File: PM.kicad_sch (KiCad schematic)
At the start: 70 parts, among them Q1 SISA14DN-T1-GE3, Q13 MMBT3904, Q2 SISA14DN-T1-GE3, Q3 SISA14DN-T1-GE3, Q4 SISA14DN-T1-GE3, Q5 CEM4435A, Q6 CH221K, SW2 SKRKAEE020, U10 LM74700QDBVRQ1, U11 CN3795, U12 XFL4020-222MEC_C122469, U4 MAX17049G+T10, U5 LM74700QDBVRQ1, U6 LM74700QDBVRQ1, U7 TPS62132RGTT, U8 LM74700QDBVRQ1, U9 XC6209F332MR-G

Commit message: [Schematic][Added] Project Architecture, connectors
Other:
- moved on the sheet: C13, C14, C15, C16, C17, C18, C19, C2, C20, C3, C37, C4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

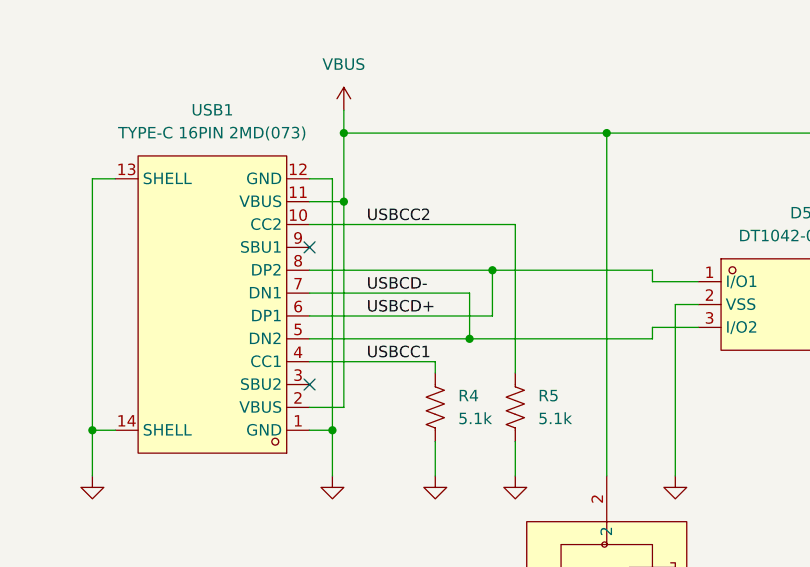
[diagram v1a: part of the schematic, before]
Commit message: [Schematic][Added] Net labels
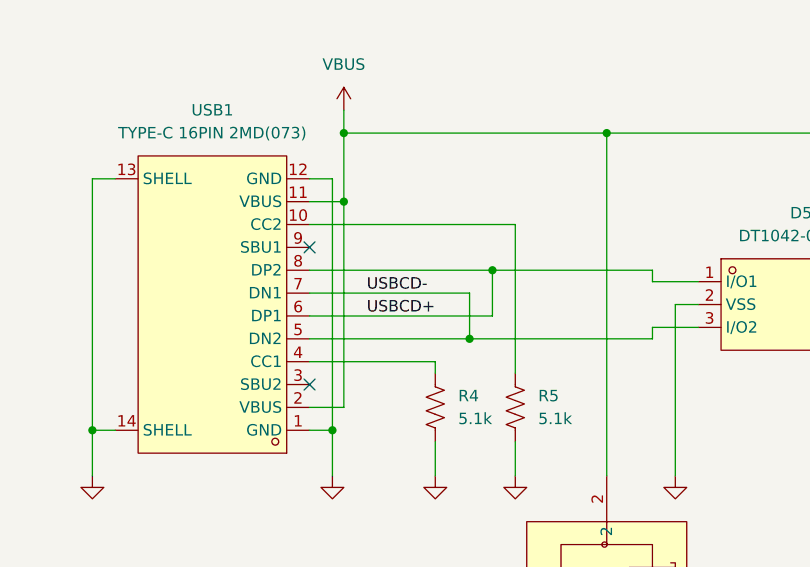
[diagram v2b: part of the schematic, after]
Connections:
- net USBCC1: no longer R4.1, USB1.4 (CC1)
- net USBCC2: no longer R5.1, USB1.10 (CC2)
- new net: R4.1, USB1.4 (CC1)
- new net: R5.1, USB1.10 (CC2)
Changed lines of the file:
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@@
-		)
-	)
-	(label "USBCC2"
-		(at 74.93 77.47 0)
-		(effects
-			(font
-				(size 1.27 1.27)
-			)
-			(justify left bottom)
 		)
 	)
@@
 		(effects
 			(font
-				(size 1.27 1.27)
-			)
-			(justify left bottom)
-		)
-	)
-	(label "USBCC1"
-		(at 74.93 92.71 0)
-		(effects
-			(font

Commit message: [PCB/SCH][Added] Preliminary version
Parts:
- removed C2, C3: 100u, Capacitor_SMD:C_1210_3225Metric, symbol Device:C
- C5: footprint Capacitor_SMD:C_0603_1608Metric -> Capacitor_SMD:C_0402_1005Metric
- R4, R5, R59, R60: footprint Resistor_SMD:R_0603_1608Metric -> Resistor_SMD:R_0402_1005Metric
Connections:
- net USBCC1: now also R4.1, USB1.4 (CC1)
- net USBCC2: now also R5.1, USB1.10 (CC2)
- net VBUS: no longer D5.5 (VCC)
- net V_BAT: now also C39.1, U9.1 (VIN), U9.3 (CE)
- net V_IN renamed V_CHRG

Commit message: [Schematic/PCB][Added] Connectors, layout, preliminar routing
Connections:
- net USBCD+: now also D5.3 (I/O2); no longer D5.1 (I/O1)
- net USBCD-: now also D5.1 (I/O1); no longer D5.3 (I/O2)
- net USBCC1 renamed CC1
- net USBCC2 renamed CC2
- no-connect marks 9 -> 10
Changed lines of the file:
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@@
 	)
 	(no_connect
+		(at 134.62 86.36)
+	)
+	(no_connect
 		(at 438.15 241.3)
 	)
@@
 	)
 	(bus_entry
+		(at 524.51 276.86)
+		(size -2.54 2.54)
+		(stroke
+			(width 0)
+			(type default)
+		)
+	)
+	(bus_entry
 		(at 524.51 241.3)
 		(size -2.54 2.54)
@@
 	)
 	(bus_entry
+		(at 524.51 274.32)
+		(size -2.54 2.54)
+		(stroke
+			(width 0)
+			(type default)
+		)
+	)
+	(bus_entry
 		(at 524.51 257.81)
 		(size -2.54 2.54)
@@
 	(wire
 		(pts
+			(xy 106.68 88.9) (xy 111.76 88.9)
+		)
+		(stroke
+			(width 0)
+			(type default)
+		)
+	)
+	(wire
+		(pts
 			(xy 502.92 73.66) (xy 514.35 73.66)
 		)
@@
 	(wire
 		(pts
-			(xy 106.68 83.82) (xy 106.68 82.55)
-		)
-		(stroke
-			(width 0)
-			(type default)
-		)
-	)
-	(wire
-		(pts
 			(xy 281.94 96.52) (xy 281.94 148.59)
 		)
@@
 	(wire
 		(pts
+			(xy 506.73 279.4) (xy 521.97 279.4)
+		)
+		(stroke
+			(width 0)
+			(type default)
+		)
+	)
+	(wire
+		(pts
 			(xy 269.24 154.94) (xy 271.78 154.94)
 		)
@@
 	(wire
 		(pts
+			(xy 107.95 83.82) (xy 111.76 83.82)
+		)
+		(stroke
+			(width 0)
+			(type default)
+		)
+	)
+	(wire
+		(pts
 			(xy 111.76 86.36) (xy 109.22 86.36)
 		)
@@
 	(wire
 		(pts
+			(xy 506.73 276.86) (xy 521.97 276.86)
+		)
+		(stroke
+			(width 0)
+			(type default)
+		)
+	)
+	(wire
+		(pts
 			(xy 236.22 90.17) (xy 240.03 90.17)
 		)
@@
 	(wire
 		(pts
-			(xy 438.15 233.68) (xy 440.69 233.68)
+			(xy 106.68 82.55) (xy 106.68 88.9)
 		)
 		(stroke
@@
 	(wire
 		(pts
-			(xy 252.73 247.65) (xy 252.73 245.11)
+			(xy 438.15 233.68) (xy 440.69 233.68)
 		)
 		(stroke
@@
 	(wire
 		(pts
-			(xy 271.78 106.68) (xy 269.24 106.68)
+			(xy 252.73 247.65) (xy 252.73 245.11)
 		)
 		(stroke
@@
 	(wire
 		(pts
-			(xy 270.51 295.91) (xy 273.05 295.91)
+			(xy 271.78 106.68) (xy 269.24 106.68)
 		)
 		(stroke
@@
 	(wire
 		(pts
-			(xy 506.73 231.14) (xy 521.97 231.14)
+			(xy 270.51 295.91) (xy 273.05 295.91)
 		)
 		(stroke
@@
 	(wire
 		(pts
-			(xy 111.76 88.9) (xy 106.68 88.9)
+			(xy 506.73 231.14) (xy 521.97 231.14)
 		)
 		(stroke
@@
 		)
 	)
+	(bus
+		(pts
+			(xy 524.51 274.32) (xy 524.51 276.86)
+		)
+		(stroke
+			(width 0)
+			(type default)
+		)
+	)
 	(wire
 		(pts
@@
 		)
 	)
+	(bus
+		(pts
+			(xy 524.51 271.78) (xy 534.67 271.78)
+		)
+		(stroke
+			(width 0)
+			(type default)
+		)
+	)
 	(wire
 		(pts
@@
 	(wire
 		(pts
-			(xy 86.36 90.17) (xy 106.68 90.17)
+			(xy 86.36 90.17) (xy 107.95 90.17)
 		)
 		(stroke
@@
 	(wire
 		(pts
-			(xy 134.62 86.36) (xy 137.16 86.36)
-		)
-		(stroke
-			(width 0)
-			(type default)
-		)
-	)
-	(wire
-		(pts
 			(xy 273.05 294.64) (xy 273.05 293.37)
 		)
@@
 	(wire
 		(pts
-			(xy 106.68 88.9) (xy 106.68 90.17)
-		)
-		(stroke
-			(width 0)
-			(type default)
-		)
-	)
-	(wire
-		(pts
 			(xy 237.49 303.53) (xy 241.3 303.53)
 		)
@@
 	(wire
 		(pts
-			(xy 111.76 83.82) (xy 106.68 83.82)
-		)
-		(stroke
-			(width 0)
-			(type default)
-		)
-	)
-	(wire
-		(pts
 			(xy 241.3 247.65) (xy 241.3 252.73)
 		)
@@
 		)
 	)
+	(bus
+		(pts
+			(xy 524.51 271.78) (xy 524.51 274.32)
+		)
+		(stroke
+			(width 0)
+			(type default)
+		)
+	)
 	(wire
 		(pts
@@
 		)
 	)
+	(bus
+		(pts
+			(xy 524.51 276.86) (xy 524.51 279.4)
+		)
+		(stroke
+			(width 0)
+			(type default)
+		)
+	)
 	(wire
 		(pts
@@
 	(wire
 		(pts
+			(xy 107.95 90.17) (xy 107.95 83.82)
+		)
+		(stroke
+			(width 0)
+			(type default)
+		)
+	)
+	(wire
+		(pts
 			(xy 240.03 101.6) (xy 240.03 106.68)
 		)
@@
 		)
 	)
-	(label "USBCC2"
-		(at 110.49 180.34 0)
+	(label "CC2"
+		(at 119.38 180.34 180)
 		(effects
 			(font
 				(size 1.27 1.27)
 			)
-			(justify left bottom)
+			(justify right bottom)
 		)
 	)
@@
 		)
 	)
-	(label "USBCC1"
-		(at 82.55 92.71 180)
+	(label "I2C_SDA"
+		(at 506.73 246.38 0)
 		(effects
 			(font
 				(size 1.27 1.27)
 			)
-			(justify right bottom)
+			(justify left bottom)
 		)
 	)
-	(label "I2C_SDA"
-		(at 506.73 246.38 0)
+	(label "CC2"
+		(at 506.73 276.86 0)
 		(effects
 			(font
@@
 		)
 	)
-	(label "USBCC1"
-		(at 110.49 182.88 0)
+	(label "CC1"
+		(at 119.38 182.88 180)
 		(effects
 			(font
 				(size 1.27 1.27)
 			)
-			(justify left bottom)
+			(justify right bottom)
 		)
 	)
@@
 		)
 	)
+	(label "CC1"
+		(at 506.73 279.4 0)
+		(effects
+			(font
+				(size 1.27 1.27)
+			)
+			(justify left bottom)
+		)
+	)
 	(label "USBCD+"
 		(at 74.93 87.63 0)
@@
 		)
 	)
-	(label "USBCC2"
+	(label "CC2"
 		(at 91.44 77.47 180)
 		(effects
@@
 		)
 	)
+	(label "CC1"
+		(at 82.55 92.71 180)
+		(effects
+			(font
+				(size 1.27 1.27)
+			)
+			(justify right bottom)
+		)
+	)
 	(label "USBCD+"
 		(at 506.73 262.89 0)
@@
 		)
 	)
+	(hierarchical_label "{CC}"
+		(shape bidirectional)
+		(at 534.67 271.78 0)
+		(effects
+			(font
+				(size 1.27 1.27)
+			)
+			(justify left)
+		)
+	)

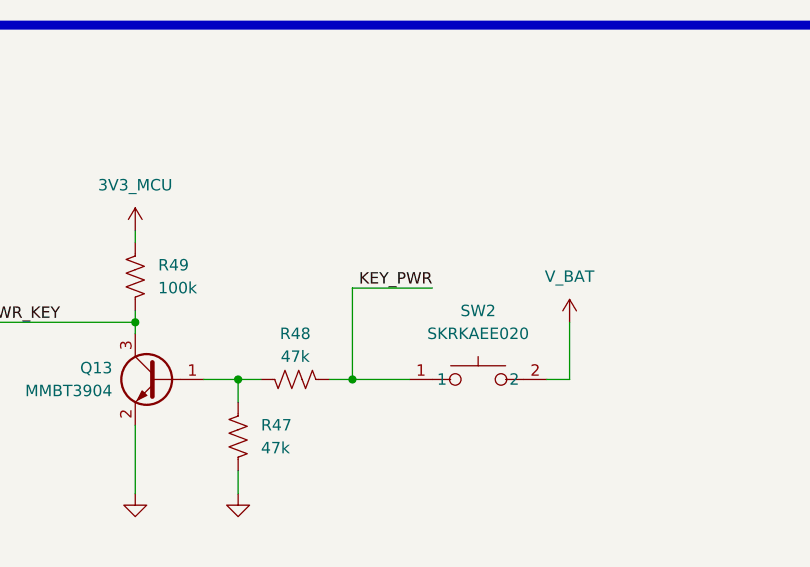
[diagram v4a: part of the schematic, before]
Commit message: [Schematic/PCB][Added] Routing almost finished
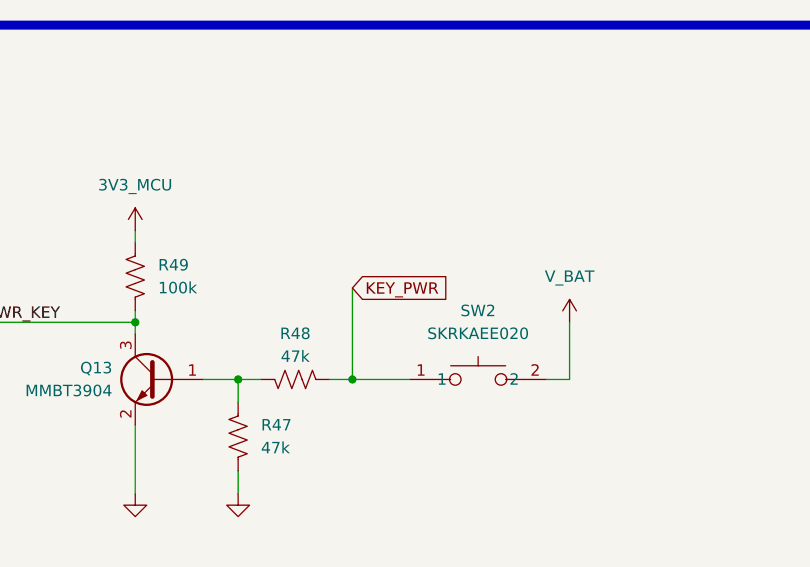
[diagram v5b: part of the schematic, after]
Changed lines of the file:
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@@
-	(wire
-		(pts
-			(xy 111.76 345.44) (xy 102.87 345.44)
-		)
-		(stroke
-			(width 0)
-			(type default)
-		)
-	)
 	(wire
 		(pts
@@
 		)
 	)
-	(label "KEY_PWR"
-		(at 111.76 345.44 180)
-		(effects
-			(font
-				(size 1.27 1.27)
-			)
-			(justify right bottom)
-		)
-	)
 	(label "LOCK_PWR"
 		(at 506.73 228.6 0)
@@
 		)
 	)
+	(global_label "KEY_PWR"
+		(shape input)
+		(at 102.87 345.44 0)
+		(fields_autoplaced yes)
+		(effects
+			(font
+				(size 1.27 1.27)
+			)
+			(justify left)
+		)
+		(property "Intersheetrefs" "${INTERSHEET_REFS}"
+			(at 114.3218 345.44 0)
+			(effects
+				(font
+					(size 1.27 1.27)
+				)
+				(justify left)
+				(hide yes)
+			)
+		)
+	)

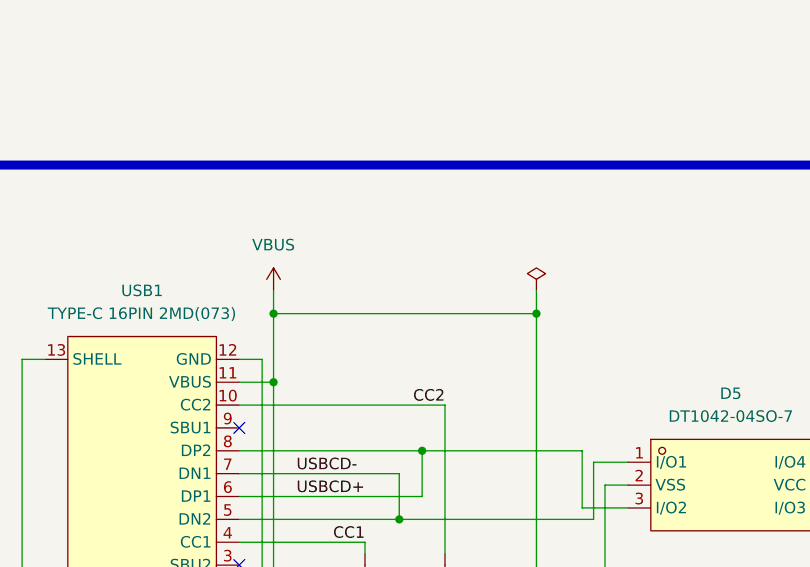
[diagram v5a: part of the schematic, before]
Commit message: [Schematic/PCB][Added] Testpoints and fabrication files test
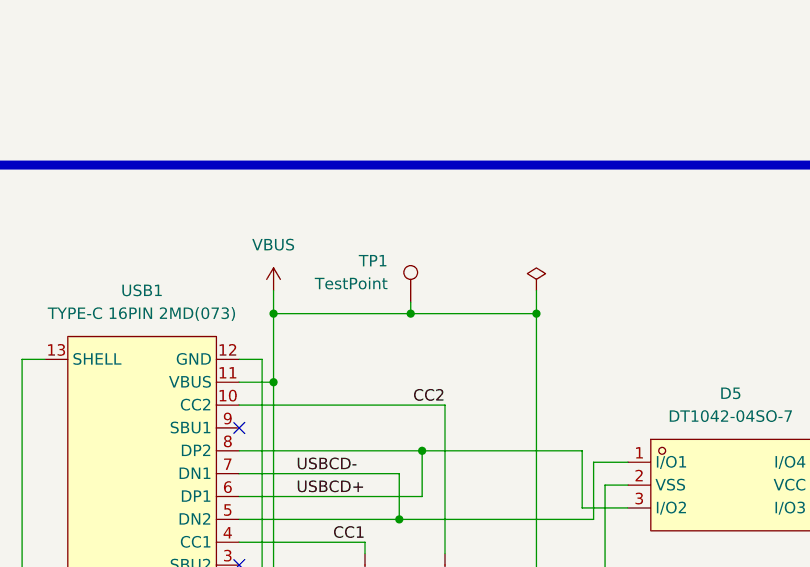
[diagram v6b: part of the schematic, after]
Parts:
- added TP1: TestPoint, tests:tp05, symbol Connector:TestPoint
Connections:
- net VBUS: now also TP1.1

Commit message: [Schematic/PCB][Added] Testpoints test 2
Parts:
- added TP10, TP2, TP3, TP4, TP5, TP6, TP7, TP8, TP9: TestPoint, tests:tp05, symbol Connector:TestPoint
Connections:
- net 3V3_FG: now also TP2.1
- net 3V3_MCU: now also TP4.1
- net PWR_KEY: now also TP8.1
- net VBUS: now also TP7.1; no longer TP1.1
- net VSUN: now also TP5.1
- net V_BAT: now also TP3.1
- net V_CHRG: now also TP6.1
- net V_MAIN: now also TP1.1
- net PWR_EN: now reaches R55.2, R56.1, U7.13 (EN)
- net PWR_EN: now also TP10.1
- net PWR_SEL: now reaches D6.1 (K), D7.1 (K), D8.1 (K), R55.1
- net PWR_SEL: now also TP9.1
